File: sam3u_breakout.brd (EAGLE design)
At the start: 50 x 50 mm, 27 parts, among them IC1 SAM3U_LQFP100

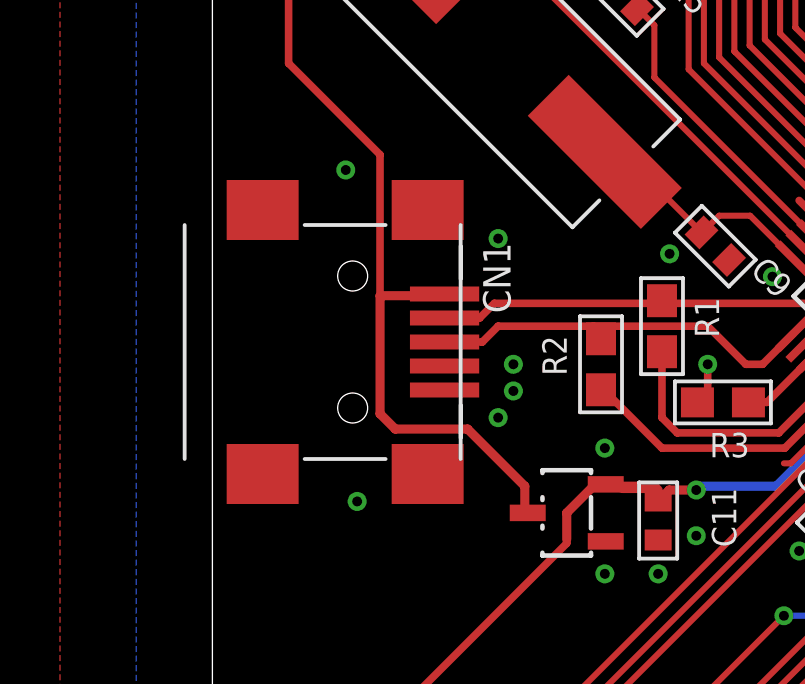
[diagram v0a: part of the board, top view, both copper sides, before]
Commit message: s/miniusb/microusb/
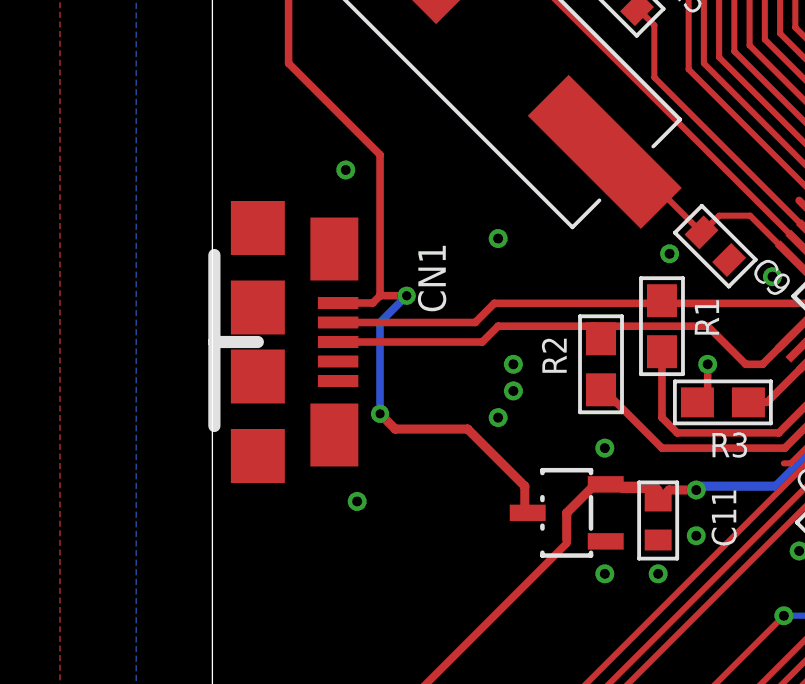
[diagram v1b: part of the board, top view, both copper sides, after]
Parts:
- CN1: device nonolith:USB-MINIB -> nonolith:USB-MICROB
- moved CN1 2.16 mm to (1.52, 23.5)
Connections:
- net 5V: now also CN1.P1; no longer CN1.VBUS
- net GND: now also CN1.P5; no longer CN1.GND
- net N$1: now also CN1.P3; no longer CN1.D+
- net N$5: now also CN1.P2; no longer CN1.D-
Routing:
- net N$5: track 14.4 -> 18.1 mm
- net N$1: track 13.3 -> 16.8 mm
- net 5V: track 33.5 -> 34.1 mm, vias 0 -> 2
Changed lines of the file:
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@@
 <?xml version="1.0" encoding="utf-8"?>
 <!DOCTYPE eagle SYSTEM "eagle.dtd">
-<eagle version="6.1">
+<eagle version="6.3">
 <drawing>
 <settings>
@@
 </class>
 </classes>
-<designrules>
+<designrules name="default">
 <description language="de">&lt;b&gt;EAGLE Design Rules&lt;/b&gt;
 &lt;p&gt;
@@
 <attribute name="VALUE" x="21.99543125" y="18.715221875" size="0.4064" layer="27" rot="R45"/>
 </element>
-<element name="CN1" library="nonolith" package="USB-MINIB" value="" x="3.675" y="23.476" smashed="yes" rot="R270">
-<attribute name="NAME" x="9.025" y="26.786" size="0.9144" layer="25" font="vector" ratio="10" rot="R270"/>
-<attribute name="VALUE" x="-2.675" y="26.786" size="1.27" layer="27" rot="R270"/>
+<element name="CN1" library="nonolith" package="USB-MICROB" value="" x="1.516" y="23.476" smashed="yes" rot="R270">
+<attribute name="NAME" x="6.866" y="26.786" size="0.9144" layer="25" font="vector" ratio="10" rot="R270"/>
+<attribute name="VALUE" x="-4.834" y="26.786" size="1.27" layer="27" rot="R270"/>
 </element>
 <element name="R1" library="nonolith" package="0603" value="39" x="14.986" y="24.003" smashed="yes" rot="R90">
@@
 <contactref element="IC1" pad="82"/>
 <contactref element="IC1" pad="72"/>
-<contactref element="CN1" pad="GND"/>
+<contactref element="CN1" pad="P5"/>
 <contactref element="R3" pad="2"/>
 <contactref element="C9" pad="2"/>
@@
 <wire x1="16.51" y1="21.805" x2="16.51" y2="22.733" width="0.254" layer="1"/>
 <via x="10.033" y="38.481" extent="1-16" drill="0.3302" shape="octagon"/>
-<contactref element="CN1" pad="GND"/>
+<contactref element="CN1" pad="P5"/>
 <polygon width="0.254" layer="1" isolate="0.254" rank="6">
 <vertex x="-5.08" y="50.8"/>
@@
 <signal name="N$5">
 <contactref element="IC1" pad="77"/>
-<contactref element="CN1" pad="D-"/>
+<contactref element="CN1" pad="P2"/>
 <contactref element="R1" pad="2"/>
 <wire x1="19.724834375" y1="23.412009375" x2="20.32" y2="24.007175" width="0.254" layer="1"/>
@@
 <wire x1="14.947" y1="24.892" x2="14.986" y2="24.853" width="0.254" layer="1"/>
 <wire x1="14.986" y1="24.765" x2="9.398" y2="24.765" width="0.254" layer="1"/>
-<wire x1="9.398" y1="24.765" x2="8.909" y2="24.276" width="0.254" layer="1"/>
-<wire x1="8.909" y1="24.276" x2="7.739" y2="24.276" width="0.254" layer="1"/>
+<wire x1="9.398" y1="24.765" x2="8.759" y2="24.126" width="0.254" layer="1"/>
+<wire x1="4.191" y1="24.126" x2="8.759" y2="24.126" width="0.254" layer="1"/>
 </signal>
 <signal name="N$1">
 <contactref element="IC1" pad="76"/>
-<contactref element="CN1" pad="D+"/>
+<contactref element="CN1" pad="P3"/>
 <contactref element="R2" pad="2"/>
 <wire x1="12.7" y1="24.003" x2="16.51" y2="24.003" width="0.254" layer="1"/>
@@
 <wire x1="17.78" y1="22.733" x2="16.51" y2="24.003" width="0.254" layer="1"/>
 <wire x1="19.37128125" y1="23.7655625" x2="18.33871875" y2="22.733" width="0.254" layer="1"/>
-<wire x1="7.739" y1="23.476" x2="8.998" y2="23.476" width="0.254" layer="1"/>
 <wire x1="8.998" y1="23.476" x2="9.525" y2="24.003" width="0.254" layer="1"/>
 <wire x1="9.525" y1="24.003" x2="12.7" y2="24.003" width="0.254" layer="1"/>
+<wire x1="4.191" y1="23.476" x2="8.998" y2="23.476" width="0.254" layer="1"/>
 </signal>
 <signal name="N$6">
@@
 </signal>
 <signal name="5V">
-<contactref element="CN1" pad="VBUS"/>
+<contactref element="CN1" pad="P1"/>
 <contactref element="U$7" pad="3"/>
-<wire x1="7.739" y1="25.076" x2="7.682" y2="25.019" width="0.3048" layer="1"/>
-<wire x1="7.682" y1="25.019" x2="5.588" y2="25.019" width="0.3048" layer="1"/>
-<wire x1="5.588" y1="25.019" x2="5.588" y2="21.082" width="0.3048" layer="1"/>
 <wire x1="5.588" y1="21.082" x2="6.096" y2="20.574" width="0.3048" layer="1"/>
 <wire x1="6.096" y1="20.574" x2="8.509" y2="20.574" width="0.3048" layer="1"/>
@@
 <wire x1="5.588" y1="29.718" x2="2.54" y2="32.766" width="0.254" layer="1"/>
 <wire x1="2.54" y1="44.412" x2="2.54" y2="32.766" width="0.254" layer="1"/>
+<wire x1="4.191" y1="24.776" x2="5.345" y2="24.776" width="0.254" layer="1"/>
+<wire x1="5.345" y1="24.776" x2="5.588" y2="25.019" width="0.254" layer="1"/>
+<via x="5.588" y="21.082" extent="1-16" drill="0.305" shape="octagon"/>
+<wire x1="5.588" y1="21.082" x2="5.588" y2="24.13" width="0.254" layer="16"/>
+<wire x1="5.588" y1="24.13" x2="6.477" y2="25.019" width="0.254" layer="16"/>
+<via x="6.477" y="25.019" extent="1-16" drill="0.305" shape="octagon"/>
+<wire x1="6.477" y1="25.019" x2="5.588" y2="25.019" width="0.254" layer="1"/>
 </signal>
 <signal name="N$3">
@@
 </signal>
 </signals>
-<errors>
-</errors>
 </board>
 </drawing>
